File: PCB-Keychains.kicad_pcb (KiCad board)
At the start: 2 copper layers, 341 x 93.3 mm, 911 parts

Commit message: Add Duck Blackbird
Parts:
- removed the REF** at (232.9, 79.1)
- removed the REF** at (236.7, 79.1)
- removed the REF** at (225.3, 79.1)
- removed the REF** at (229.1, 79.1)
- removed the REF** at (215.3, 79.1)
- removed the REF** at (219.1, 79.1)
- removed the REF** at (207.6, 79.1)
- removed the REF** at (211.5, 79.1)
- removed the REF** at (115.3, 79.1)
- removed the REF** at (149.5, 79.1)
- removed the REF** at (130.5, 79.1)
- removed the REF** at (122.9, 79.1)
- removed the REF** at (126.7, 79.1)
- removed the REF** at (138.1, 79.1)
- removed the REF** at (141.9, 79.1)
- removed the REF** at (157.2, 79.1)
- removed the REF** at (153.4, 79.1)
- removed the REF** at (145.7, 79.1)
- removed the REF** at (119.1, 79.1)
- removed the REF** at (134.3, 79.1)
- removed the REF** at (115.3, 82.9)
- removed the REF** at (149.5, 82.9)
- removed the REF** at (130.5, 82.9)
- removed the REF** at (122.9, 82.9)
- removed the REF** at (126.7, 82.9)
- removed the REF** at (138.1, 82.9)
- removed the REF** at (141.9, 82.9)
- removed the REF** at (157.2, 82.9)
- removed the REF** at (153.4, 82.9)
- removed the REF** at (145.7, 82.9)
- removed the REF** at (119.1, 82.9)
- removed the REF** at (134.3, 82.9)
- removed the REF** at (191.5, 103.8)
- removed the REF** at (191.5, 96.2)
- removed the REF** at (191.5, 88.6)
- removed the REF** at (191.5, 92.4)
- removed the REF** at (191.5, 100.0)
- removed the REF** at (195.3, 88.6)
- removed the REF** at (183.8, 103.8)
- removed the REF** at (183.8, 96.2)
- removed the REF** at (183.8, 88.6)
- removed the REF** at (183.8, 92.4)
- removed the REF** at (183.8, 100.0)
- removed the REF** at (187.6, 88.6)
- removed the REF** at (296.7, 67.6)
- removed the REF** at (302.9, 64.6)
- removed the REF** at (288.1, 59.1)
- added REF**: Pad-1.25U, locallib:Pad-1.25U, F.Cu at (68.1, 129.5)
- added REF**: Pad-1U, locallib:Pad-1U, F.Cu at (48.6, 121.9)
- added REF**: Pad-1U, locallib:Pad-1U, F.Cu at (35.2, 125.7)
- added REF**: Pad-1U, locallib:Pad-1U, F.Cu at (60.0, 121.9)
- added REF**: Pad-1U, locallib:Pad-1U, F.Cu at (62.9, 118.1)
- added REF**: Pad-1U, locallib:Pad-1U, F.Cu at (32.4, 118.1)
- added REF**: Pad-1U, locallib:Pad-1U, F.Cu at (47.6, 118.1)
- added REF**: Pad-1U, locallib:Pad-1U, F.Cu at (52.4, 121.9)
- added REF**: Pad-1U, locallib:Pad-1U, F.Cu at (19.1, 114.3)
- added REF**: Pad-1U, locallib:Pad-1U, F.Cu at (223.8, 124.3)
- added REF**: Pad-1U, locallib:Pad-1U, F.Cu at (31.4, 125.7)
- added REF**: Pad-7U, locallib:Pad-7U, F.Cu at (43.8, 129.5)
- added REF**: Pad-1U, locallib:Pad-1U, F.Cu at (63.8, 129.5)
- added REF**: Pad-1.75U, locallib:Pad-1.75U, F.Cu at (20.5, 121.9)
- added REF**: Pad-1U, locallib:Pad-1U, F.Cu at (44.8, 121.9)
- added REF**: Pad-1.5U, locallib:Pad-1.5U, F.Cu at (71.4, 118.1)
- added REF**: Pad-1U, locallib:Pad-1U, F.Cu at (41.0, 121.9)
- added REF**: Pad-1U, locallib:Pad-1U, F.Cu at (37.1, 121.9)
- added REF**: Pad-1U, locallib:Pad-1U, F.Cu at (40.0, 118.1)
- added REF**: Pad-1U, locallib:Pad-1U, F.Cu at (29.5, 121.9)
- added REF**: Pad-1U, locallib:Pad-1U, F.Cu at (127.2, 79.1)
- added REF**: Pad-1U, locallib:Pad-1U, F.Cu at (131.0, 79.1)
- added REF**: Pad-1U, locallib:Pad-1U, F.Cu at (119.5, 79.1)
- added REF**: Pad-1U, locallib:Pad-1U, F.Cu at (55.2, 118.1)
- added REF**: Pad-1U, locallib:Pad-1U, F.Cu at (123.3, 79.1)
- added REF**: Pad-1U, locallib:Pad-1U, F.Cu at (109.5, 79.1)
- added REF**: Pad-1U, locallib:Pad-1U, F.Cu at (113.3, 79.1)
- added REF**: Pad-1U, locallib:Pad-1U, F.Cu at (101.9, 79.1)
- added REF**: Pad-1U, locallib:Pad-1U, F.Cu at (105.7, 79.1)
- added REF**: Pad-1U, locallib:Pad-1U, F.Cu at (201.9, 75.7)
- added REF**: Pad-1U, locallib:Pad-1U, F.Cu at (236.2, 75.7)
- added REF**: Pad-1U, locallib:Pad-1U, F.Cu at (217.2, 75.7)
- added REF**: Pad-1U, locallib:Pad-1U, F.Cu at (209.6, 75.7)
- added REF**: Pad-1U, locallib:Pad-1U, F.Cu at (213.4, 75.7)
- added REF**: Pad-1U, locallib:Pad-1U, F.Cu at (25.7, 121.9)
- added REF**: Pad-1U, locallib:Pad-1U, F.Cu at (224.8, 75.7)
- added REF**: Pad-1U, locallib:Pad-1U, F.Cu at (228.6, 75.7)
- added REF**: Pad-1U, locallib:Pad-1U, F.Cu at (243.8, 75.7)
- added REF**: Pad-1U, locallib:Pad-1U, F.Cu at (240.0, 75.7)
- added REF**: Pad-1U, locallib:Pad-1U, F.Cu at (232.4, 75.7)
- added REF**: Pad-1U, locallib:Pad-1U, F.Cu at (205.7, 75.7)
- added REF**: Pad-1U, locallib:Pad-1U, F.Cu at (221.0, 75.7)
- added REF**: Pad-1U, locallib:Pad-1U, F.Cu at (201.9, 79.5)
- added REF**: Pad-1U, locallib:Pad-1U, F.Cu at (236.2, 79.5)
- added REF**: Pad-1U, locallib:Pad-1U, F.Cu at (217.2, 79.5)
- added REF**: Pad-1U, locallib:Pad-1U, F.Cu at (49.5, 114.3)
- added REF**: Pad-1U, locallib:Pad-1U, F.Cu at (209.6, 79.5)
- added REF**: Pad-1U, locallib:Pad-1U, F.Cu at (213.4, 79.5)
- added REF**: Pad-1U, locallib:Pad-1U, F.Cu at (224.8, 79.5)
- added REF**: Pad-1U, locallib:Pad-1U, F.Cu at (228.6, 79.5)
- added REF**: Pad-1U, locallib:Pad-1U, F.Cu at (243.8, 79.5)
- added REF**: Pad-1U, locallib:Pad-1U, F.Cu at (240.0, 79.5)
- added REF**: Pad-1U, locallib:Pad-1U, F.Cu at (232.4, 79.5)
- added REF**: Pad-1U, locallib:Pad-1U, F.Cu at (205.7, 79.5)
- added REF**: Pad-1U, locallib:Pad-1U, F.Cu at (221.0, 79.5)
- added REF**: Pad-1U, locallib:Pad-1U, F.Cu at (278.1, 100.5)
- added REF**: Pad-1.25U, locallib:Pad-1.25U, F.Cu at (59.5, 129.5)
- added REF**: Pad-1U, locallib:Pad-1U, F.Cu at (42.9, 125.7)
- added REF**: Pad-1U, locallib:Pad-1U, F.Cu at (278.1, 92.9)
- added REF**: Pad-1U, locallib:Pad-1U, F.Cu at (278.1, 85.2)
- added REF**: Pad-1U, locallib:Pad-1U, F.Cu at (278.1, 89.1)
- added REF**: Pad-1U, locallib:Pad-1U, F.Cu at (278.1, 96.7)
- added REF**: Pad-1U, locallib:Pad-1U, F.Cu at (281.9, 85.2)
- added REF**: Pad-1U, locallib:Pad-1U, F.Cu at (270.5, 100.5)
- added REF**: Pad-1U, locallib:Pad-1U, F.Cu at (270.5, 92.9)
- added REF**: Pad-1U, locallib:Pad-1U, F.Cu at (270.5, 85.2)
- added REF**: Pad-2U, locallib:Pad-2U, F.Cu at (70.5, 114.3)
- added REF**: Pad-1U, locallib:Pad-1U, F.Cu at (270.5, 89.1)
- added REF**: Pad-1U, locallib:Pad-1U, F.Cu at (270.5, 96.7)
- added REF**: Pad-1U, locallib:Pad-1U, F.Cu at (274.3, 85.2)
- added REF**: Pad-1U, locallib:Pad-1U, F.Cu at (81.9, 114.3)
- added REF**: Pad-2.25U, locallib:Pad-2.25U, F.Cu at (70.0, 121.9)
- added REF**: Pad-1U, locallib:Pad-1U, F.Cu at (73.3, 130.5)
- added REF**: Pad-2.25U, locallib:Pad-2.25U, F.Cu at (21.4, 125.7)
- added REF**: Pad-1U, locallib:Pad-1U, F.Cu at (54.3, 125.7)
- added REF**: Pad-1U, locallib:Pad-1U, F.Cu at (89.5, 114.3)
- added REF**: Pad-1U, locallib:Pad-1U, F.Cu at (81.0, 130.5)
- added REF**: Pad-1U, locallib:Pad-1U, F.Cu at (50.5, 125.7)
- added REF**: Pad-1U, locallib:Pad-1U, F.Cu at (59.1, 118.1)
- added REF**: Pad-1U, locallib:Pad-1U, F.Cu at (77.2, 126.7)
- added REF**: Pad-1U, locallib:Pad-1U, F.Cu at (56.2, 121.9)
- added REF**: Pad-1U, locallib:Pad-1U, F.Cu at (46.7, 125.7)
- added REF**: Pad-1U, locallib:Pad-1U, F.Cu at (22.9, 114.3)
- added REF**: Pad-1U, locallib:Pad-1U, F.Cu at (26.7, 114.3)
- added REF**: Pad-1U, locallib:Pad-1U, F.Cu at (77.2, 130.5)
- added REF**: Pad-1U, locallib:Pad-1U, F.Cu at (39.1, 125.7)
- added REF**: Pad-1U, locallib:Pad-1U, F.Cu at (85.7, 118.1)
- added REF**: Pad-1U, locallib:Pad-1U, F.Cu at (81.9, 118.1)
- added REF**: Pad-1U, locallib:Pad-1U, F.Cu at (89.5, 118.1)
- added REF**: Pad-1U, locallib:Pad-1U, F.Cu at (63.8, 121.9)
- added REF**: Pad-1U, locallib:Pad-1U, F.Cu at (24.8, 118.1)
- added REF**: Pad-1U, locallib:Pad-1U, F.Cu at (38.1, 114.3)
- added REF**: Pad-1U, locallib:Pad-1U, F.Cu at (85.7, 114.3)
- added REF**: Pad-1U, locallib:Pad-1U, F.Cu at (57.1, 114.3)
- added REF**: Pad-1U, locallib:Pad-1U, F.Cu at (30.5, 114.3)
- added REF**: Pad-1U, locallib:Pad-1U, F.Cu at (61.0, 114.3)
- added REF**: Pad-1U, locallib:Pad-1U, F.Cu at (51.4, 118.1)
- added REF**: Pad-1U, locallib:Pad-1U, F.Cu at (89.5, 129.5)
- added REF**: Pad-1U, locallib:Pad-1U, F.Cu at (85.7, 129.5)
- added REF**: Pad-1U, locallib:Pad-1U, F.Cu at (34.3, 114.3)
- added REF**: Pad-1U, locallib:Pad-1U, F.Cu at (58.1, 125.7)
- added REF**: Pad-1U, locallib:Pad-1U, F.Cu at (28.6, 118.1)
- added REF**: Pad-1U, locallib:Pad-1U, F.Cu at (45.7, 114.3)
- added REF**: Pad-1U, locallib:Pad-1U, F.Cu at (43.8, 118.1)
- added REF**: Pad-1U, locallib:Pad-1U, F.Cu at (93.3, 114.3)
- added REF**: Pad-1U, locallib:Pad-1U, F.Cu at (53.3, 114.3)
- added REF**: Pad-1U, locallib:Pad-1U, F.Cu at (66.7, 118.1)
- added REF**: Pad-1U, locallib:Pad-1U, F.Cu at (85.7, 121.9)
- added REF**: Pad-1U, locallib:Pad-1U, F.Cu at (89.5, 125.7)
- added REF**: Pad-1U, locallib:Pad-1U, F.Cu at (93.3, 121.9)
- added REF**: Pad-1U, locallib:Pad-1U, F.Cu at (41.9, 114.3)
- added REF**: Pad-1U, locallib:Pad-1U, F.Cu at (27.6, 125.7)
- added REF**: Pad-1U, locallib:Pad-1U, F.Cu at (85.7, 125.7)
- added REF**: Pad-1U, locallib:Pad-1U, F.Cu at (64.8, 114.3)
- added REF**: Pad-1.5U, locallib:Pad-1.5U, F.Cu at (20.0, 118.1)
- added REF**: Pad-1U, locallib:Pad-1U, F.Cu at (81.9, 121.9)
- added REF**: Pad-1U, locallib:Pad-1U, F.Cu at (81.9, 125.7)
- added REF**: Pad-1U, locallib:Pad-1U, F.Cu at (36.2, 118.1)
- added REF**: Pad-1U, locallib:Pad-1U, F.Cu at (93.3, 118.1)
- added REF**: Pad-1U, locallib:Pad-1U, F.Cu at (89.5, 121.9)
- added REF**: Pad-2U, locallib:Pad-2U, F.Cu at (93.3, 127.6)
- added REF**: Pad-1U, locallib:Pad-1U, F.Cu at (61.9, 125.7)
- added REF**: Pad-1U, locallib:Pad-1U, F.Cu at (33.3, 121.9)
- added REF**: Pad-2U, locallib:Pad-2U, F.Cu at (232.4, 132.9)
- added REF**: Pad-1U, locallib:Pad-1U, F.Cu at (238.6, 129.9)
- added REF**: Pad-2.75U, locallib:Pad-2.75U, F.Cu at (69.1, 125.7)
- added REF**: Pad-1U, locallib:Pad-1U, F.Cu at (77.2, 114.3)
- added REF**: Pad-1U, locallib:Pad-1U, F.Cu at (77.2, 118.1)
- added REF**: Pad-1.25U, locallib:Pad-1.25U, F.Cu at (19.5, 129.5)
- added REF**: Pad-1U, locallib:Pad-1U, F.Cu at (23.8, 129.5)
- added REF**: Pad-1.25U, locallib:Pad-1.25U, F.Cu at (28.1, 129.5)
- moved REF** 105.7 mm to (149.5, 89.1)
- moved REF** 105.7 mm to (147.6, 85.2)
- moved REF** 105.7 mm to (145.7, 89.1)
- moved REF** 105.7 mm to (131.4, 92.9)
- moved REF** 105.7 mm to (154.3, 96.7)
- moved REF** 105.7 mm to (150.5, 100.5)
- moved REF** 105.7 mm to (107.6, 89.1)
- moved REF** 105.7 mm to (154.3, 100.5)
- moved REF** 105.7 mm to (143.8, 85.2)
- moved REF** 105.7 mm to (129.5, 96.7)
- moved REF** 105.7 mm to (166.7, 100.5)
- moved REF** 105.7 mm to (158.6, 79.1)
- moved REF** 105.7 mm to (166.2, 79.1)
- moved REF** 105.7 mm to (162.4, 79.1)
- moved REF** 105.7 mm to (154.8, 79.1)
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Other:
- board size 341 x 93.3 mm -> 278.1 x 127.6 mm
- board text added: "Mechanical Keyboards Blackbird"

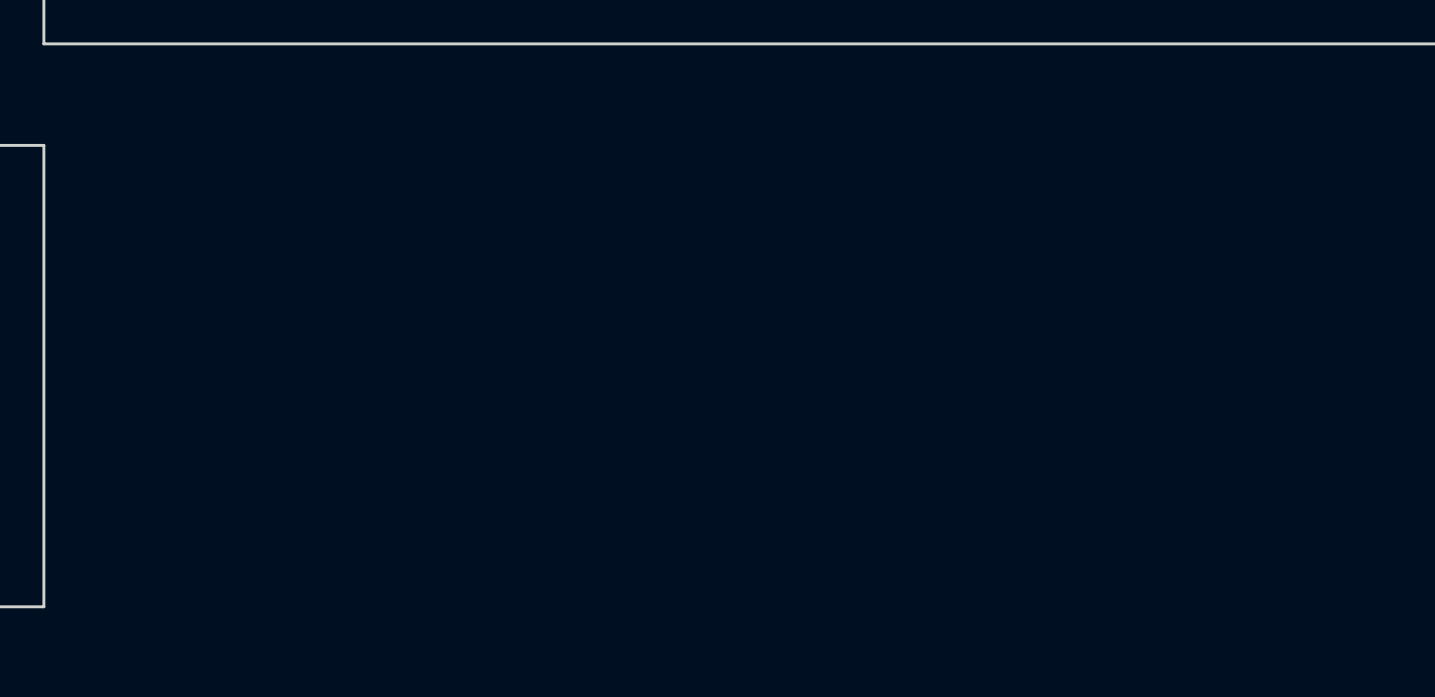
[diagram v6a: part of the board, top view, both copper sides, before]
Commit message: Add HHKB
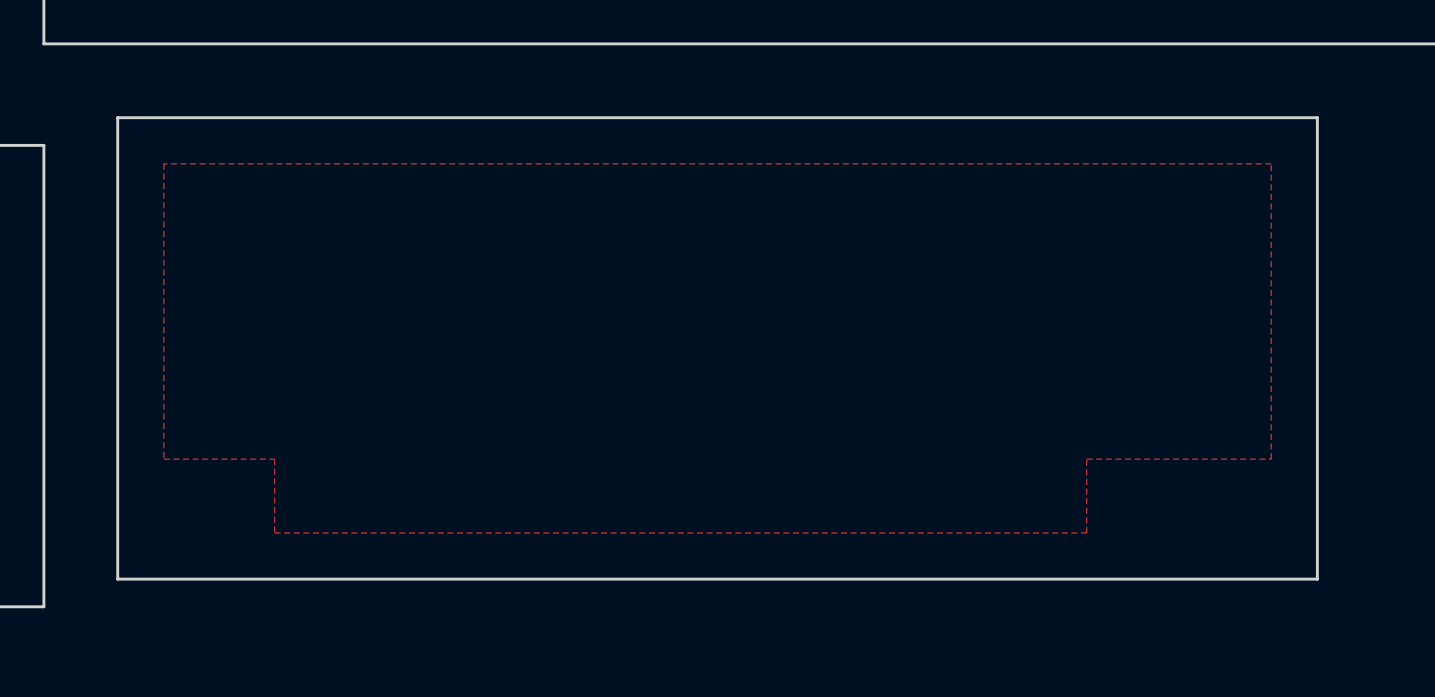
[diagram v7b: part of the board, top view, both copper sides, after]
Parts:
- added REF**: Pad-1U, locallib:Pad-1U, F.Cu at (137.2, 124.3)
- added REF**: Pad-1.5U, locallib:Pad-1.5U, F.Cu at (158.1, 116.7)
- added REF**: Pad-1U, locallib:Pad-1U, F.Cu at (155.3, 112.9)
- added REF**: Pad-1U, locallib:Pad-1U, F.Cu at (159.1, 112.9)
- added REF**: Pad-1.75U, locallib:Pad-1.75U, F.Cu at (153.8, 124.3)
- added REF**: Pad-1U, locallib:Pad-1U, F.Cu at (159.1, 124.3)
- added REF**: Pad-6U, locallib:Pad-6U, F.Cu at (130.5, 128.1)
- added REF**: Pad-2.25U, locallib:Pad-2.25U, F.Cu at (156.7, 120.5)
- added REF**: Pad-2.25U, locallib:Pad-2.25U, F.Cu at (108.1, 124.3)
- added REF**: Pad-1.5U, locallib:Pad-1.5U, F.Cu at (116.2, 128.1)
- added REF**: Pad-1U, locallib:Pad-1U, F.Cu at (111.4, 128.1)
- added REF**: Pad-1U, locallib:Pad-1U, F.Cu at (105.7, 112.9)
- added REF**: Pad-1U, locallib:Pad-1U, F.Cu at (117.2, 112.9)
- added REF**: Pad-1U, locallib:Pad-1U, F.Cu at (113.3, 112.9)
- added REF**: Pad-1U, locallib:Pad-1U, F.Cu at (121.0, 112.9)
- added REF**: Pad-1U, locallib:Pad-1U, F.Cu at (147.6, 112.9)
- added REF**: Pad-1U, locallib:Pad-1U, F.Cu at (149.5, 128.1)
- added REF**: Pad-1U, locallib:Pad-1U, F.Cu at (148.6, 124.3)
- added REF**: Pad-1U, locallib:Pad-1U, F.Cu at (141.9, 116.7)
- added REF**: Pad-1U, locallib:Pad-1U, F.Cu at (134.3, 116.7)
- added REF**: Pad-1U, locallib:Pad-1U, F.Cu at (123.8, 120.5)
- added REF**: Pad-1U, locallib:Pad-1U, F.Cu at (135.3, 120.5)
- added REF**: Pad-1U, locallib:Pad-1U, F.Cu at (131.4, 120.5)
- added REF**: Pad-1U, locallib:Pad-1U, F.Cu at (112.4, 120.5)
- added REF**: Pad-1U, locallib:Pad-1U, F.Cu at (150.5, 120.5)
- added REF**: Pad-1U, locallib:Pad-1U, F.Cu at (120.0, 120.5)
- added REF**: Pad-1U, locallib:Pad-1U, F.Cu at (118.1, 124.3)
- added REF**: Pad-1U, locallib:Pad-1U, F.Cu at (125.7, 124.3)
- added REF**: Pad-1U, locallib:Pad-1U, F.Cu at (144.8, 124.3)
- added REF**: Pad-1U, locallib:Pad-1U, F.Cu at (119.1, 116.7)
- added REF**: Pad-1U, locallib:Pad-1U, F.Cu at (145.7, 116.7)
- added REF**: Pad-1U, locallib:Pad-1U, F.Cu at (126.7, 116.7)
- added REF**: Pad-1U, locallib:Pad-1U, F.Cu at (142.9, 120.5)
- added REF**: Pad-1U, locallib:Pad-1U, F.Cu at (128.6, 112.9)
- added REF**: Pad-1U, locallib:Pad-1U, F.Cu at (132.4, 112.9)
- added REF**: Pad-1U, locallib:Pad-1U, F.Cu at (153.4, 116.7)
- added REF**: Pad-1U, locallib:Pad-1U, F.Cu at (127.6, 120.5)
- added REF**: Pad-1U, locallib:Pad-1U, F.Cu at (138.1, 116.7)
- added REF**: Pad-1U, locallib:Pad-1U, F.Cu at (133.3, 124.3)
- added REF**: Pad-1U, locallib:Pad-1U, F.Cu at (140.0, 112.9)
- added REF**: Pad-1U, locallib:Pad-1U, F.Cu at (114.3, 124.3)
- added REF**: Pad-1U, locallib:Pad-1U, F.Cu at (115.3, 116.7)
- added REF**: Pad-1U, locallib:Pad-1U, F.Cu at (130.5, 116.7)
- added REF**: Pad-1U, locallib:Pad-1U, F.Cu at (122.9, 116.7)
- added REF**: Pad-1U, locallib:Pad-1U, F.Cu at (116.2, 120.5)
- added REF**: Pad-1U, locallib:Pad-1U, F.Cu at (136.2, 112.9)
- added REF**: Pad-1U, locallib:Pad-1U, F.Cu at (139.1, 120.5)
- added REF**: Pad-1U, locallib:Pad-1U, F.Cu at (149.5, 116.7)
- added REF**: Pad-1U, locallib:Pad-1U, F.Cu at (121.9, 124.3)
- added REF**: Pad-1U, locallib:Pad-1U, F.Cu at (141.0, 124.3)
- added REF**: Pad-1U, locallib:Pad-1U, F.Cu at (109.5, 112.9)
- added REF**: Pad-1U, locallib:Pad-1U, F.Cu at (146.7, 120.5)
- added REF**: Pad-1U, locallib:Pad-1U, F.Cu at (124.8, 112.9)
- added REF**: Pad-1U, locallib:Pad-1U, F.Cu at (143.8, 112.9)
- added REF**: Pad-1U, locallib:Pad-1U, F.Cu at (151.4, 112.9)
- added REF**: Pad-1U, locallib:Pad-1U, F.Cu at (111.4, 116.7)
- added REF**: Pad-1.5U, locallib:Pad-1.5U, F.Cu at (144.8, 128.1)
- added REF**: Pad-1U, locallib:Pad-1U, F.Cu at (129.5, 124.3)
- added REF**: Pad-1.5U, locallib:Pad-1.5U, F.Cu at (106.7, 116.7)
- added REF**: Pad-1.75U, locallib:Pad-1.75U, F.Cu at (107.2, 120.5)
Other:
- outline, holes or cut-outs redrawn
- board text added: "Mechanical Keyboards HHKB"

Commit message: Add XD75RE, 40%, 96%, etc
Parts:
- removed the REF** at (109.5, 34.3)
- removed the REF** at (232.4, 132.9)
- removed the REF** at (238.6, 129.9)
- removed the REF** at (223.8, 124.3)
- removed the REF** at (127.2, 79.1)
- removed the REF** at (131.0, 79.1)
- removed the REF** at (119.5, 79.1)
- removed the REF** at (123.3, 79.1)
- removed the REF** at (109.5, 79.1)
- removed the REF** at (113.3, 79.1)
- removed the REF** at (101.9, 79.1)
- removed the REF** at (105.7, 79.1)
- removed the REF** at (201.9, 75.7)
- removed the REF** at (236.2, 75.7)
- removed the REF** at (217.2, 75.7)
- removed the REF** at (209.6, 75.7)
- removed the REF** at (213.4, 75.7)
- removed the REF** at (224.8, 75.7)
- removed the REF** at (228.6, 75.7)
- removed the REF** at (243.8, 75.7)
- removed the REF** at (240.0, 75.7)
- removed the REF** at (232.4, 75.7)
- removed the REF** at (205.7, 75.7)
- removed the REF** at (221.0, 75.7)
- removed the REF** at (201.9, 79.5)
- removed the REF** at (236.2, 79.5)
- removed the REF** at (217.2, 79.5)
- removed the REF** at (209.6, 79.5)
- removed the REF** at (213.4, 79.5)
- removed the REF** at (224.8, 79.5)
- removed the REF** at (228.6, 79.5)
- removed the REF** at (243.8, 79.5)
- removed the REF** at (240.0, 79.5)
- removed the REF** at (232.4, 79.5)
- removed the REF** at (205.7, 79.5)
- removed the REF** at (221.0, 79.5)
- removed the REF** at (278.1, 100.5)
- removed the REF** at (278.1, 92.9)
- removed the REF** at (278.1, 85.2)
- removed the REF** at (278.1, 89.1)
- removed the REF** at (278.1, 96.7)
- removed the REF** at (281.9, 85.2)
- removed the REF** at (270.5, 100.5)
- removed the REF** at (270.5, 92.9)
- removed the REF** at (270.5, 85.2)
- removed the REF** at (270.5, 89.1)
- removed the REF** at (270.5, 96.7)
- removed the REF** at (274.3, 85.2)
- removed the REF** at (174.3, 58.1)
- removed the REF** at (204.8, 58.1)
- removed the REF** at (193.4, 58.1)
- removed the REF** at (208.6, 58.1)
- removed the REF** at (197.2, 58.1)
- removed the REF** at (178.1, 58.1)
- removed the REF** at (170.5, 58.1)
- removed the REF** at (201.0, 58.1)
- removed the REF** at (181.9, 58.1)
- removed the REF** at (166.7, 58.1)
- removed the REF** at (174.3, 54.3)
- removed the REF** at (204.8, 54.3)
- removed the REF** at (189.5, 54.3)
- removed the REF** at (193.4, 54.3)
- removed the REF** at (208.6, 54.3)
- removed the REF** at (197.2, 54.3)
- removed the REF** at (178.1, 54.3)
- removed the REF** at (170.5, 54.3)
- removed the REF** at (201.0, 54.3)
- removed the REF** at (181.9, 54.3)
- removed the REF** at (185.7, 54.3)
- removed the REF** at (166.7, 54.3)
- removed the REF** at (174.3, 50.5)
- removed the REF** at (204.8, 50.5)
- removed the REF** at (189.5, 50.5)
- removed the REF** at (193.4, 50.5)
- removed the REF** at (208.6, 50.5)
- removed the REF** at (197.2, 50.5)
- removed the REF** at (178.1, 50.5)
- removed the REF** at (170.5, 50.5)
- removed the REF** at (201.0, 50.5)
- removed the REF** at (181.9, 50.5)
- removed the REF** at (185.7, 50.5)
- removed the REF** at (166.7, 50.5)
- removed the REF** at (174.3, 46.7)
- removed the REF** at (204.8, 46.7)
- removed the REF** at (189.5, 46.7)
- removed the REF** at (193.4, 46.7)
- removed the REF** at (208.6, 46.7)
- removed the REF** at (197.2, 46.7)
- removed the REF** at (178.1, 46.7)
- removed the REF** at (170.5, 46.7)
- removed the REF** at (201.0, 46.7)
- removed the REF** at (181.9, 46.7)
- removed the REF** at (185.7, 46.7)
- removed the REF** at (166.7, 46.7)
- removed the REF** at (130.5, 59.1)
- removed the REF** at (214.3, 26.7)
- removed the REF** at (64.8, 46.7)
- removed the REF** at (72.4, 46.7)
- removed the REF** at (68.6, 46.7)
- removed the REF** at (61.0, 46.7)
- removed the REF** at (47.6, 46.7)
- removed the REF** at (55.2, 46.7)
- removed the REF** at (51.4, 46.7)
- removed the REF** at (43.8, 46.7)
- removed the REF** at (84.8, 66.7)
- removed the REF** at (81.0, 66.7)
- removed the REF** at (77.2, 66.7)
- removed the REF** at (81.0, 62.9)
- removed the REF** at (84.8, 55.2)
- removed the REF** at (81.0, 55.2)
- removed the REF** at (77.2, 55.2)
- removed the REF** at (84.8, 51.4)
- removed the REF** at (81.0, 51.4)
- removed the REF** at (77.2, 51.4)
- added REF**: Pad-1U, locallib:Pad-1U, F.Cu at (161.0, 171.4)
- added REF**: Pad-1U, locallib:Pad-1U, F.Cu at (157.2, 167.6)
- added REF**: Pad-1U, locallib:Pad-1U, F.Cu at (232.4, 172.4)
- added REF**: Pad-1U, locallib:Pad-1U, F.Cu at (195.3, 48.6)
- added REF**: Pad-1U, locallib:Pad-1U, F.Cu at (176.2, 48.6)
- added REF**: Pad-1U, locallib:Pad-1U, F.Cu at (168.6, 48.6)
- added REF**: Pad-1U, locallib:Pad-1U, F.Cu at (199.1, 48.6)
- added REF**: Pad-1U, locallib:Pad-1U, F.Cu at (180.0, 48.6)
- added REF**: Pad-1U, locallib:Pad-1U, F.Cu at (183.8, 48.6)
- added REF**: Pad-1U, locallib:Pad-1U, F.Cu at (164.8, 48.6)
- added REF**: Pad-1U, locallib:Pad-1U, F.Cu at (172.4, 44.8)
- added REF**: Pad-1U, locallib:Pad-1U, F.Cu at (202.9, 44.8)
- added REF**: Pad-1U, locallib:Pad-1U, F.Cu at (187.6, 44.8)
- added REF**: Pad-1U, locallib:Pad-1U, F.Cu at (248.6, 176.2)
- added REF**: Pad-1U, locallib:Pad-1U, F.Cu at (191.5, 44.8)
- added REF**: Pad-1U, locallib:Pad-1U, F.Cu at (206.7, 44.8)
- added REF**: Pad-1U, locallib:Pad-1U, F.Cu at (195.3, 44.8)
- added REF**: Pad-1U, locallib:Pad-1U, F.Cu at (176.2, 44.8)
- added REF**: Pad-1U, locallib:Pad-1U, F.Cu at (168.6, 44.8)
- added REF**: Pad-1U, locallib:Pad-1U, F.Cu at (199.1, 44.8)
- added REF**: Pad-1U, locallib:Pad-1U, F.Cu at (180.0, 44.8)
- added REF**: Pad-1U, locallib:Pad-1U, F.Cu at (183.8, 44.8)
- added REF**: Pad-1U, locallib:Pad-1U, F.Cu at (164.8, 44.8)
- added REF**: Pad-1U, locallib:Pad-1U, F.Cu at (233.4, 176.2)
- added REF**: Pad-1U, locallib:Pad-1U, F.Cu at (243.8, 172.4)
- added REF**: Pad-1U, locallib:Pad-1U, F.Cu at (220.0, 180.0)
- added REF**: Pad-1U, locallib:Pad-1U, F.Cu at (221.0, 172.4)
- added REF**: Pad-1U, locallib:Pad-1U, F.Cu at (236.2, 172.4)
- added REF**: Pad-1U, locallib:Pad-1U, F.Cu at (228.6, 172.4)
- added REF**: Pad-1U, locallib:Pad-1U, F.Cu at (221.9, 176.2)
- added REF**: Pad-1U, locallib:Pad-1U, F.Cu at (128.6, 57.1)
- added REF**: Pad-1U, locallib:Pad-1U, F.Cu at (244.8, 176.2)
- added REF**: Pad-1U, locallib:Pad-1U, F.Cu at (212.4, 24.8)
- added REF**: Pad-1U, locallib:Pad-1U, F.Cu at (157.2, 163.8)
- added REF**: Pad-1U, locallib:Pad-1U, F.Cu at (227.6, 180.0)
- added REF**: Pad-1U, locallib:Pad-1U, F.Cu at (217.2, 172.4)
- added REF**: Pad-1U, locallib:Pad-1U, F.Cu at (66.7, 172.4)
- added REF**: Pad-1U, locallib:Pad-1U, F.Cu at (70.5, 172.4)
- added REF**: Pad-1U, locallib:Pad-1U, F.Cu at (47.6, 172.4)
- added REF**: Pad-1U, locallib:Pad-1U, F.Cu at (17.1, 172.4)
- added REF**: Pad-1U, locallib:Pad-1U, F.Cu at (21.0, 172.4)
- added REF**: Pad-1U, locallib:Pad-1U, F.Cu at (74.3, 172.4)
- added REF**: Pad-1U, locallib:Pad-1U, F.Cu at (55.2, 172.4)
- added REF**: Pad-1U, locallib:Pad-1U, F.Cu at (36.2, 172.4)
- added REF**: Pad-1U, locallib:Pad-1U, F.Cu at (161.0, 175.3)
- added REF**: Pad-1U, locallib:Pad-1U, F.Cu at (78.1, 172.4)
- added REF**: Pad-1U, locallib:Pad-1U, F.Cu at (81.9, 172.4)
- added REF**: Pad-1U, locallib:Pad-1U, F.Cu at (24.8, 172.4)
- added REF**: Pad-1U, locallib:Pad-1U, F.Cu at (28.6, 172.4)
- added REF**: Pad-1U, locallib:Pad-1U, F.Cu at (59.1, 172.4)
- added REF**: Pad-1U, locallib:Pad-1U, F.Cu at (62.9, 172.4)
- added REF**: Pad-1U, locallib:Pad-1U, F.Cu at (51.4, 172.4)
- added REF**: Pad-1U, locallib:Pad-1U, F.Cu at (32.4, 172.4)
- added REF**: Pad-1U, locallib:Pad-1U, F.Cu at (43.8, 172.4)
- added REF**: Pad-1U, locallib:Pad-1U, F.Cu at (85.7, 172.4)
- added REF**: Pad-1U, locallib:Pad-1U, F.Cu at (157.2, 175.3)
- added REF**: Pad-1U, locallib:Pad-1U, F.Cu at (40.0, 172.4)
- added REF**: Pad-1U, locallib:Pad-1U, F.Cu at (57.1, 180.0)
- added REF**: Pad-1U, locallib:Pad-1U, F.Cu at (62.9, 44.8)
- added REF**: Pad-1U, locallib:Pad-1U, F.Cu at (70.5, 44.8)
- added REF**: Pad-1U, locallib:Pad-1U, F.Cu at (66.7, 44.8)
- added REF**: Pad-1U, locallib:Pad-1U, F.Cu at (59.1, 44.8)
- added REF**: Pad-1U, locallib:Pad-1U, F.Cu at (45.7, 44.8)
- added REF**: Pad-1U, locallib:Pad-1U, F.Cu at (53.3, 44.8)
- added REF**: Pad-1U, locallib:Pad-1U, F.Cu at (49.5, 44.8)
- added REF**: Pad-1U, locallib:Pad-1U, F.Cu at (61.9, 183.8)
- added REF**: Pad-1U, locallib:Pad-1U, F.Cu at (41.9, 44.8)
- added REF**: Pad-1U, locallib:Pad-1U, F.Cu at (82.9, 64.8)
- added REF**: Pad-1U, locallib:Pad-1U, F.Cu at (79.1, 64.8)
- added REF**: Pad-1U, locallib:Pad-1U, F.Cu at (75.2, 64.8)
- added REF**: Pad-1U, locallib:Pad-1U, F.Cu at (79.1, 61.0)
- added REF**: Pad-1U, locallib:Pad-1U, F.Cu at (56.2, 187.6)
- added REF**: Pad-1U, locallib:Pad-1U, F.Cu at (82.9, 53.3)
- added REF**: Pad-1U, locallib:Pad-1U, F.Cu at (79.1, 53.3)
- added REF**: Pad-1U, locallib:Pad-1U, F.Cu at (75.2, 53.3)
- added REF**: Pad-1U, locallib:Pad-1U, F.Cu at (82.9, 49.5)
- added REF**: Pad-1U, locallib:Pad-1U, F.Cu at (79.1, 49.5)
- added REF**: Pad-1U, locallib:Pad-1U, F.Cu at (75.2, 49.5)
- added REF**: Pad-1U, locallib:Pad-1U, F.Cu at (25.7, 187.6)
- added REF**: Pad-1U, locallib:Pad-1U, F.Cu at (60.0, 187.6)
- added REF**: Pad-1.5U, locallib:Pad-1.5U, F.Cu at (56.2, 191.5)
- added REF**: Pad-1U, locallib:Pad-1U, F.Cu at (31.4, 183.8)
- added REF**: Pad-1U, locallib:Pad-1U, F.Cu at (46.7, 183.8)
- added REF**: Pad-1U, locallib:Pad-1U, F.Cu at (33.3, 187.6)
- added REF**: Pad-1U, locallib:Pad-1U, F.Cu at (157.2, 179.1)
- added REF**: Pad-1U, locallib:Pad-1U, F.Cu at (58.1, 183.8)
- added REF**: Pad-1U, locallib:Pad-1U, F.Cu at (61.0, 180.0)
- added REF**: Pad-1U, locallib:Pad-1U, F.Cu at (30.5, 180.0)
- added REF**: Pad-1U, locallib:Pad-1U, F.Cu at (45.7, 180.0)
- added REF**: Pad-1U, locallib:Pad-1U, F.Cu at (50.5, 183.8)
- added REF**: Pad-1U, locallib:Pad-1U, F.Cu at (17.1, 176.2)
- added REF**: Pad-1U, locallib:Pad-1U, F.Cu at (29.5, 187.6)
- added REF**: Pad-6U, locallib:Pad-6U, F.Cu at (107.6, 32.4)
- added REF**: Pad-7U, locallib:Pad-7U, F.Cu at (40.0, 191.5)
- added REF**: Pad-1.75U, locallib:Pad-1.75U, F.Cu at (18.6, 183.8)
- added REF**: Pad-2U, locallib:Pad-2U, F.Cu at (230.5, 131.0)
- added REF**: Pad-1U, locallib:Pad-1U, F.Cu at (42.9, 183.8)
- added REF**: Pad-1U, locallib:Pad-1U, F.Cu at (236.7, 128.0)
- added REF**: Pad-1U, locallib:Pad-1U, F.Cu at (164.8, 163.8)
- added REF**: Pad-1.5U, locallib:Pad-1.5U, F.Cu at (18.1, 191.5)
- added REF**: Pad-2U, locallib:Pad-2U, F.Cu at (89.5, 160.0)
- added REF**: Pad-1U, locallib:Pad-1U, F.Cu at (22.9, 160.0)
- added REF**: Pad-1U, locallib:Pad-1U, F.Cu at (64.8, 160.0)
- added REF**: Pad-1.5U, locallib:Pad-1.5U, F.Cu at (254.3, 148.6)
- added REF**: Pad-1.5U, locallib:Pad-1.5U, F.Cu at (69.5, 180.0)
- added REF**: Pad-1.25U, locallib:Pad-1.25U, F.Cu at (254.8, 152.4)
- added REF**: Pad-1.25U, locallib:Pad-1.25U, F.Cu at (211.9, 152.4)
- added REF**: Pad-1.25U, locallib:Pad-1.25U, F.Cu at (227.2, 160.0)
- added REF**: Pad-2U, locallib:Pad-2U, F.Cu at (233.4, 160.0)
- added REF**: Pad-1.25U, locallib:Pad-1.25U, F.Cu at (239.6, 160.0)
- added REF**: Pad-1.25U, locallib:Pad-1.25U, F.Cu at (211.9, 183.8)
- added REF**: Pad-1.25U, locallib:Pad-1.25U, F.Cu at (220.5, 183.8)
- added REF**: Pad-6U, locallib:Pad-6U, F.Cu at (234.3, 183.8)
- added REF**: Pad-1.75U, locallib:Pad-1.75U, F.Cu at (251.9, 180.0)
- added REF**: Pad-1U, locallib:Pad-1U, F.Cu at (257.2, 180.0)
- added REF**: Pad-1U, locallib:Pad-1U, F.Cu at (39.1, 183.8)
- added REF**: Pad-1U, locallib:Pad-1U, F.Cu at (35.2, 183.8)
- added REF**: Pad-1U, locallib:Pad-1U, F.Cu at (38.1, 180.0)
- added REF**: Pad-1U, locallib:Pad-1U, F.Cu at (27.6, 183.8)
- added REF**: Pad-1U, locallib:Pad-1U, F.Cu at (53.3, 180.0)
- added REF**: Pad-1U, locallib:Pad-1U, F.Cu at (23.8, 183.8)
- added REF**: Pad-1U, locallib:Pad-1U, F.Cu at (47.6, 176.2)
- added REF**: Pad-1U, locallib:Pad-1U, F.Cu at (41.0, 187.6)
- added REF**: Pad-1U, locallib:Pad-1U, F.Cu at (126.7, 175.3)
- added REF**: Pad-2U, locallib:Pad-2U, F.Cu at (68.6, 176.2)
- added REF**: Pad-1U, locallib:Pad-1U, F.Cu at (74.3, 176.2)
- added REF**: Pad-2.25U, locallib:Pad-2.25U, F.Cu at (68.1, 183.8)
- added REF**: Pad-1U, locallib:Pad-1U, F.Cu at (66.7, 191.5)
- added REF**: Pad-2.25U, locallib:Pad-2.25U, F.Cu at (19.5, 187.6)
- added REF**: Pad-1U, locallib:Pad-1U, F.Cu at (52.4, 187.6)
- added REF**: Pad-1U, locallib:Pad-1U, F.Cu at (81.9, 176.2)
- added REF**: Pad-1U, locallib:Pad-1U, F.Cu at (74.3, 191.5)
- added REF**: Pad-1U, locallib:Pad-1U, F.Cu at (48.6, 187.6)
- added REF**: Pad-1.5U, locallib:Pad-1.5U, F.Cu at (23.8, 191.5)
- added REF**: Pad-1U, locallib:Pad-1U, F.Cu at (141.9, 175.3)
- added REF**: Pad-1U, locallib:Pad-1U, F.Cu at (70.5, 187.6)
- added REF**: Pad-1U, locallib:Pad-1U, F.Cu at (54.3, 183.8)
- added REF**: Pad-1U, locallib:Pad-1U, F.Cu at (44.8, 187.6)
- added REF**: Pad-1U, locallib:Pad-1U, F.Cu at (21.0, 176.2)
- added REF**: Pad-1U, locallib:Pad-1U, F.Cu at (24.8, 176.2)
- added REF**: Pad-1U, locallib:Pad-1U, F.Cu at (70.5, 191.5)
- added REF**: Pad-1U, locallib:Pad-1U, F.Cu at (37.1, 187.6)
- added REF**: Pad-1U, locallib:Pad-1U, F.Cu at (78.1, 180.0)
- added REF**: Pad-1.5U, locallib:Pad-1.5U, F.Cu at (61.9, 191.5)
- added REF**: Pad-1U, locallib:Pad-1U, F.Cu at (74.3, 180.0)
- added REF**: Pad-1U, locallib:Pad-1U, F.Cu at (134.3, 179.1)
- added REF**: Pad-1U, locallib:Pad-1U, F.Cu at (81.9, 180.0)
- added REF**: Pad-1U, locallib:Pad-1U, F.Cu at (22.9, 180.0)
- added REF**: Pad-1U, locallib:Pad-1U, F.Cu at (36.2, 176.2)
- added REF**: Pad-1U, locallib:Pad-1U, F.Cu at (78.1, 176.2)
- added REF**: Pad-1U, locallib:Pad-1U, F.Cu at (55.2, 176.2)
- added REF**: Pad-1U, locallib:Pad-1U, F.Cu at (28.6, 176.2)
- added REF**: Pad-1U, locallib:Pad-1U, F.Cu at (59.1, 176.2)
- added REF**: Pad-1U, locallib:Pad-1U, F.Cu at (49.5, 180.0)
- added REF**: Pad-1U, locallib:Pad-1U, F.Cu at (81.9, 191.5)
- added REF**: Pad-1U, locallib:Pad-1U, F.Cu at (78.1, 191.5)
- added REF**: Pad-1U, locallib:Pad-1U, F.Cu at (149.5, 179.1)
- added REF**: Pad-1U, locallib:Pad-1U, F.Cu at (32.4, 176.2)
- added REF**: Pad-1U, locallib:Pad-1U, F.Cu at (26.7, 180.0)
- added REF**: Pad-1U, locallib:Pad-1U, F.Cu at (43.8, 176.2)
- added REF**: Pad-1U, locallib:Pad-1U, F.Cu at (41.9, 180.0)
- added REF**: Pad-1U, locallib:Pad-1U, F.Cu at (85.7, 176.2)
- added REF**: Pad-1U, locallib:Pad-1U, F.Cu at (51.4, 176.2)
- added REF**: Pad-1U, locallib:Pad-1U, F.Cu at (64.8, 180.0)
- added REF**: Pad-1U, locallib:Pad-1U, F.Cu at (78.1, 183.8)
- added REF**: Pad-1U, locallib:Pad-1U, F.Cu at (81.9, 187.6)
- added REF**: Pad-1U, locallib:Pad-1U, F.Cu at (85.7, 183.8)
- added REF**: Pad-1U, locallib:Pad-1U, F.Cu at (164.8, 167.6)
- added REF**: Pad-1U, locallib:Pad-1U, F.Cu at (138.1, 179.1)
- added REF**: Pad-1U, locallib:Pad-1U, F.Cu at (40.0, 176.2)
- added REF**: Pad-1U, locallib:Pad-1U, F.Cu at (78.1, 187.6)
- added REF**: Pad-1U, locallib:Pad-1U, F.Cu at (62.9, 176.2)
- added REF**: Pad-1.5U, locallib:Pad-1.5U, F.Cu at (18.1, 180.0)
- added REF**: Pad-1U, locallib:Pad-1U, F.Cu at (74.3, 183.8)
- added REF**: Pad-1U, locallib:Pad-1U, F.Cu at (74.3, 187.6)
- added REF**: Pad-1U, locallib:Pad-1U, F.Cu at (34.3, 180.0)
- added REF**: Pad-1U, locallib:Pad-1U, F.Cu at (85.7, 180.0)
- added REF**: Pad-1U, locallib:Pad-1U, F.Cu at (81.9, 183.8)
- added REF**: Pad-2U, locallib:Pad-2U, F.Cu at (85.7, 189.5)
- added REF**: Pad-1U, locallib:Pad-1U, F.Cu at (115.3, 175.3)
- added REF**: Pad-1.75U, locallib:Pad-1.75U, F.Cu at (65.2, 187.6)
- added REF**: Pad-1U, locallib:Pad-1U, F.Cu at (251.5, 160.0)
- added REF**: Pad-1U, locallib:Pad-1U, F.Cu at (243.8, 160.0)
- added REF**: Pad-1U, locallib:Pad-1U, F.Cu at (255.3, 160.0)
- added REF**: Pad-1U, locallib:Pad-1U, F.Cu at (247.7, 160.0)
- added REF**: Pad-1U, locallib:Pad-1U, F.Cu at (215.3, 160.0)
- added REF**: Pad-1U, locallib:Pad-1U, F.Cu at (211.5, 160.0)
- added REF**: Pad-1U, locallib:Pad-1U, F.Cu at (222.9, 160.0)
- added REF**: Pad-1U, locallib:Pad-1U, F.Cu at (219.1, 160.0)
- added REF**: Pad-1U, locallib:Pad-1U, F.Cu at (236.2, 156.2)
- added REF**: Pad-1U, locallib:Pad-1U, F.Cu at (153.4, 175.3)
- added REF**: Pad-1U, locallib:Pad-1U, F.Cu at (217.2, 156.2)
- added REF**: Pad-1U, locallib:Pad-1U, F.Cu at (251.5, 156.2)
- added REF**: Pad-1.5U, locallib:Pad-1.5U, F.Cu at (212.4, 156.2)
- added REF**: Pad-1U, locallib:Pad-1U, F.Cu at (255.3, 156.2)
- added REF**: Pad-1U, locallib:Pad-1U, F.Cu at (240.0, 156.2)
- added REF**: Pad-1U, locallib:Pad-1U, F.Cu at (221.0, 156.2)
- added REF**: Pad-1U, locallib:Pad-1U, F.Cu at (224.8, 156.2)
- added REF**: Pad-1U, locallib:Pad-1U, F.Cu at (232.4, 156.2)
- added REF**: Pad-1U, locallib:Pad-1U, F.Cu at (228.6, 156.2)
- added REF**: Pad-1U, locallib:Pad-1U, F.Cu at (243.8, 156.2)
- added REF**: Pad-1U, locallib:Pad-1U, F.Cu at (119.1, 175.3)
- added REF**: Pad-1U, locallib:Pad-1U, F.Cu at (247.7, 156.2)
- added REF**: Pad-1U, locallib:Pad-1U, F.Cu at (235.3, 152.4)
- added REF**: Pad-1U, locallib:Pad-1U, F.Cu at (220.0, 152.4)
- added REF**: Pad-1U, locallib:Pad-1U, F.Cu at (216.2, 152.4)
- added REF**: Pad-1U, locallib:Pad-1U, F.Cu at (231.5, 152.4)
- added REF**: Pad-1U, locallib:Pad-1U, F.Cu at (250.5, 152.4)
- added REF**: Pad-1U, locallib:Pad-1U, F.Cu at (246.7, 152.4)
- added REF**: Pad-1U, locallib:Pad-1U, F.Cu at (239.1, 152.4)
- added REF**: Pad-1U, locallib:Pad-1U, F.Cu at (242.9, 152.4)
- added REF**: Pad-1U, locallib:Pad-1U, F.Cu at (227.6, 152.4)
- added REF**: Pad-1U, locallib:Pad-1U, F.Cu at (119.1, 179.1)
- added REF**: Pad-1U, locallib:Pad-1U, F.Cu at (223.8, 152.4)
- added REF**: Pad-1U, locallib:Pad-1U, F.Cu at (211.5, 148.6)
- added REF**: Pad-1U, locallib:Pad-1U, F.Cu at (222.9, 148.6)
- added REF**: Pad-1U, locallib:Pad-1U, F.Cu at (219.1, 148.6)
- added REF**: Pad-1U, locallib:Pad-1U, F.Cu at (226.7, 148.6)
- added REF**: Pad-1U, locallib:Pad-1U, F.Cu at (234.3, 148.6)
- added REF**: Pad-1U, locallib:Pad-1U, F.Cu at (238.1, 148.6)
- added REF**: Pad-1U, locallib:Pad-1U, F.Cu at (245.7, 148.6)
- added REF**: Pad-1U, locallib:Pad-1U, F.Cu at (241.9, 148.6)
- added REF**: Pad-1U, locallib:Pad-1U, F.Cu at (215.3, 148.6)
- added REF**: Pad-1U, locallib:Pad-1U, F.Cu at (145.7, 179.1)
- added REF**: Pad-1U, locallib:Pad-1U, F.Cu at (230.5, 148.6)
- added REF**: Pad-1U, locallib:Pad-1U, F.Cu at (249.6, 148.6)
- added REF**: Pad-1U, locallib:Pad-1U, F.Cu at (177.2, 111.0)
- added REF**: Pad-1U, locallib:Pad-1U, F.Cu at (177.2, 118.6)
- added REF**: Pad-1U, locallib:Pad-1U, F.Cu at (173.4, 118.6)
- added REF**: Pad-1U, locallib:Pad-1U, F.Cu at (177.2, 122.4)
- added REF**: Pad-1U, locallib:Pad-1U, F.Cu at (169.5, 118.6)
- added REF**: Pad-1U, locallib:Pad-1U, F.Cu at (169.5, 114.8)
- added REF**: Pad-1U, locallib:Pad-1U, F.Cu at (181.0, 111.0)
- added REF**: Pad-1U, locallib:Pad-1U, F.Cu at (173.4, 122.4)
- added REF**: Pad-1U, locallib:Pad-1U, F.Cu at (130.5, 175.3)
- added REF**: Pad-2U, locallib:Pad-2U, F.Cu at (181.0, 124.3)
- added REF**: Pad-1U, locallib:Pad-1U, F.Cu at (169.5, 122.4)
- added REF**: Pad-1U, locallib:Pad-1U, F.Cu at (169.5, 111.0)
- added REF**: Pad-1U, locallib:Pad-1U, F.Cu at (177.2, 126.2)
- added REF**: Pad-1U, locallib:Pad-1U, F.Cu at (177.2, 114.8)
- added REF**: Pad-2U, locallib:Pad-2U, F.Cu at (181.0, 116.7)
- added REF**: Pad-1U, locallib:Pad-1U, F.Cu at (173.4, 114.8)
- added REF**: Pad-2U, locallib:Pad-2U, F.Cu at (171.4, 126.2)
- added REF**: Pad-1U, locallib:Pad-1U, F.Cu at (173.4, 111.0)
- added REF**: Pad-1U, locallib:Pad-1U, F.Cu at (187.6, 147.6)
- added REF**: Pad-1U, locallib:Pad-1U, F.Cu at (130.5, 179.1)
- added REF**: Pad-1U, locallib:Pad-1U, F.Cu at (195.3, 147.6)
- added REF**: Pad-1U, locallib:Pad-1U, F.Cu at (191.5, 151.4)
- added REF**: Pad-1U, locallib:Pad-1U, F.Cu at (187.6, 151.4)
- added REF**: Pad-1U, locallib:Pad-1U, F.Cu at (195.3, 151.4)
- added REF**: Pad-1U, locallib:Pad-1U, F.Cu at (191.5, 147.6)
- added REF**: Pad-1U, locallib:Pad-1U, F.Cu at (187.6, 143.8)
- added REF**: Pad-1U, locallib:Pad-1U, F.Cu at (195.3, 140.0)
- added REF**: Pad-1U, locallib:Pad-1U, F.Cu at (187.6, 140.0)
- added REF**: Pad-1U, locallib:Pad-1U, F.Cu at (191.5, 143.8)
- added REF**: Pad-1U, locallib:Pad-1U, F.Cu at (191.5, 140.0)
- added REF**: Pad-1U, locallib:Pad-1U, F.Cu at (149.5, 175.3)
- added REF**: Pad-1U, locallib:Pad-1U, F.Cu at (199.1, 147.6)
- added REF**: Pad-1U, locallib:Pad-1U, F.Cu at (195.3, 143.8)
- added REF**: Pad-1U, locallib:Pad-1U, F.Cu at (199.1, 140.0)
- added REF**: Pad-1U, locallib:Pad-1U, F.Cu at (199.1, 151.4)
- added REF**: Pad-1U, locallib:Pad-1U, F.Cu at (199.1, 143.8)
- added REF**: Pad-1U, locallib:Pad-1U, F.Cu at (111.4, 147.6)
- added REF**: Pad-1U, locallib:Pad-1U, F.Cu at (119.1, 147.6)
- added REF**: Pad-1U, locallib:Pad-1U, F.Cu at (115.3, 151.4)
- added REF**: Pad-1U, locallib:Pad-1U, F.Cu at (111.4, 151.4)
- added REF**: Pad-1U, locallib:Pad-1U, F.Cu at (119.1, 151.4)
- added REF**: Pad-1U, locallib:Pad-1U, F.Cu at (134.3, 175.3)
- added REF**: Pad-1U, locallib:Pad-1U, F.Cu at (115.3, 147.6)
- added REF**: Pad-1U, locallib:Pad-1U, F.Cu at (111.4, 143.8)
- added REF**: Pad-1U, locallib:Pad-1U, F.Cu at (119.1, 140.0)
- added REF**: Pad-1U, locallib:Pad-1U, F.Cu at (111.4, 140.0)
- added REF**: Pad-1U, locallib:Pad-1U, F.Cu at (115.3, 143.8)
- added REF**: Pad-1U, locallib:Pad-1U, F.Cu at (115.3, 140.0)
- added REF**: Pad-1U, locallib:Pad-1U, F.Cu at (122.9, 147.6)
- added REF**: Pad-1U, locallib:Pad-1U, F.Cu at (119.1, 143.8)
- added REF**: Pad-1U, locallib:Pad-1U, F.Cu at (122.9, 140.0)
- added REF**: Pad-1U, locallib:Pad-1U, F.Cu at (122.9, 151.4)
- added REF**: Pad-1U, locallib:Pad-1U, F.Cu at (161.0, 179.1)
- added REF**: Pad-1U, locallib:Pad-1U, F.Cu at (111.4, 175.3)
- added REF**: Pad-1U, locallib:Pad-1U, F.Cu at (122.9, 143.8)
- added REF**: Pad-1U, locallib:Pad-1U, F.Cu at (160.0, 147.6)
- added REF**: Pad-1U, locallib:Pad-1U, F.Cu at (176.2, 151.4)
- added REF**: Pad-1U, locallib:Pad-1U, F.Cu at (148.6, 147.6)
- added REF**: Pad-1U, locallib:Pad-1U, F.Cu at (156.2, 147.6)
- added REF**: Pad-1.5U, locallib:Pad-1.5U, F.Cu at (181.0, 151.4)
- added REF**: Pad-1U, locallib:Pad-1U, F.Cu at (163.8, 147.6)
- added REF**: Pad-1.5U, locallib:Pad-1.5U, F.Cu at (171.4, 151.4)
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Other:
- board size 278.1 x 127.6 mm -> 278.1 x 182.9 mm
- board text added: "Mechanical Keyboards 40% ANSI"
- board text added: "Mechanical Keyboards 96% ANSI"
- board text added: "Mechanical Keyboards ANSI Fullsize"
- board text added: "Mechanical Keyboards Breadstick"
- board text added: "Mechanical Keyboards UT47"
- board text added: "Mechanical Keyboards XD75RE"
